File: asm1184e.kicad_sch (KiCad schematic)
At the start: 96 parts, among them J1 Bus_PCI_Express_x16, J2 Bus_PCI_Express_x16, J3 Bus_PCI_Express_x16, J4 Bus_PCI_Express_x16, J5 Bus_PCI_Express_x1, U12 ASM1184

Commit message: Add files via upload
version 1 done. hardware test and verification up next.
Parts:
- C10, C16: value 100n -> 12p
- R38: value 0 -> NC
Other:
- title: (none) -> asm1184e
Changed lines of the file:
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@@
 	(generator_version "9.0")
 	(paper "A3")
+	(title_block
+		(title "asm1184e")
+		(date "2025-04-09")
+		(rev "1")
+	)
 	(text "IS:\n0.1  -> 1A\n0.05 -> 2.5A\nFB:\n1.25V\n(1+R1/R2)*1.25=Vout"
 		(exclude_from_sim no)
@@
 			)
 		)
-		(property "Value" "100n"
+		(property "Value" "12p"
 			(at 69.342 224.79 90)
 			(effects
@@
 			)
 		)
-		(property "Value" "100n"
+		(property "Value" "12p"
 			(at 69.342 198.12 90)
 			(effects
@@
 		(dnp no)
 		(property "Reference" "R38"
-			(at 100.584 212.344 90)
+			(at 99.7575 212.34 90)
 			(effects
 				(font
@@
 			)
 		)
-		(property "Value" "0"
-			(at 99.822 214.63 90)
+		(property "Value" "NC"
+			(at 103.124 212.344 90)
 			(effects
 				(font
@@
 		(dnp no)
 		(property "Reference" "C15"
-			(at 60.452 215.9 90)
+			(at 61.0247 216.0039 90)
 			(effects
 				(font
@@
 		(dnp no)
 		(property "Reference" "C14"
-			(at 31.75 217.932 90)
+			(at 31.7992 218.8462 90)
 			(effects
 				(font
@@
 		(dnp no)
 		(property "Reference" "C18"
-			(at 96.901 217.8628 0)
+			(at 97.028 219.964 0)
 			(effects
 				(font
@@
 		)
 		(property "Value" "22u"
-			(at 96.901 220.2871 0)
+			(at 97.028 222.3883 0)
 			(effects
 				(font

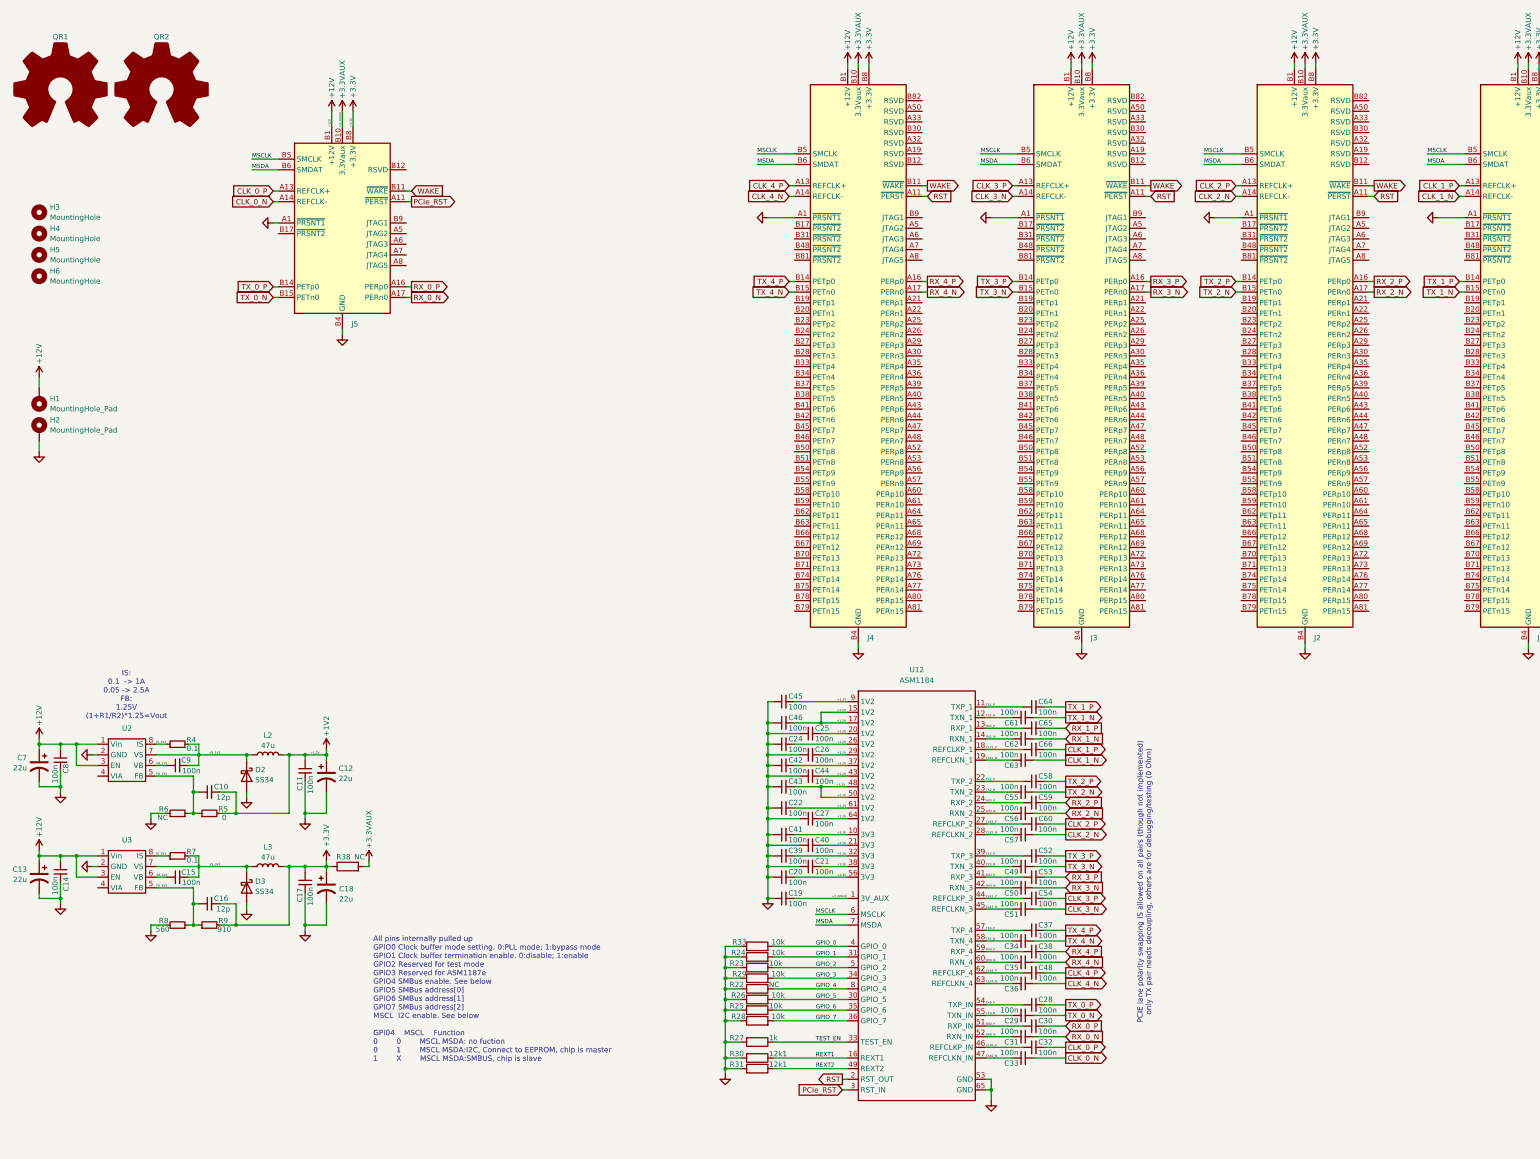
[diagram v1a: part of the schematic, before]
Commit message: added extra NC capacitors because why not.
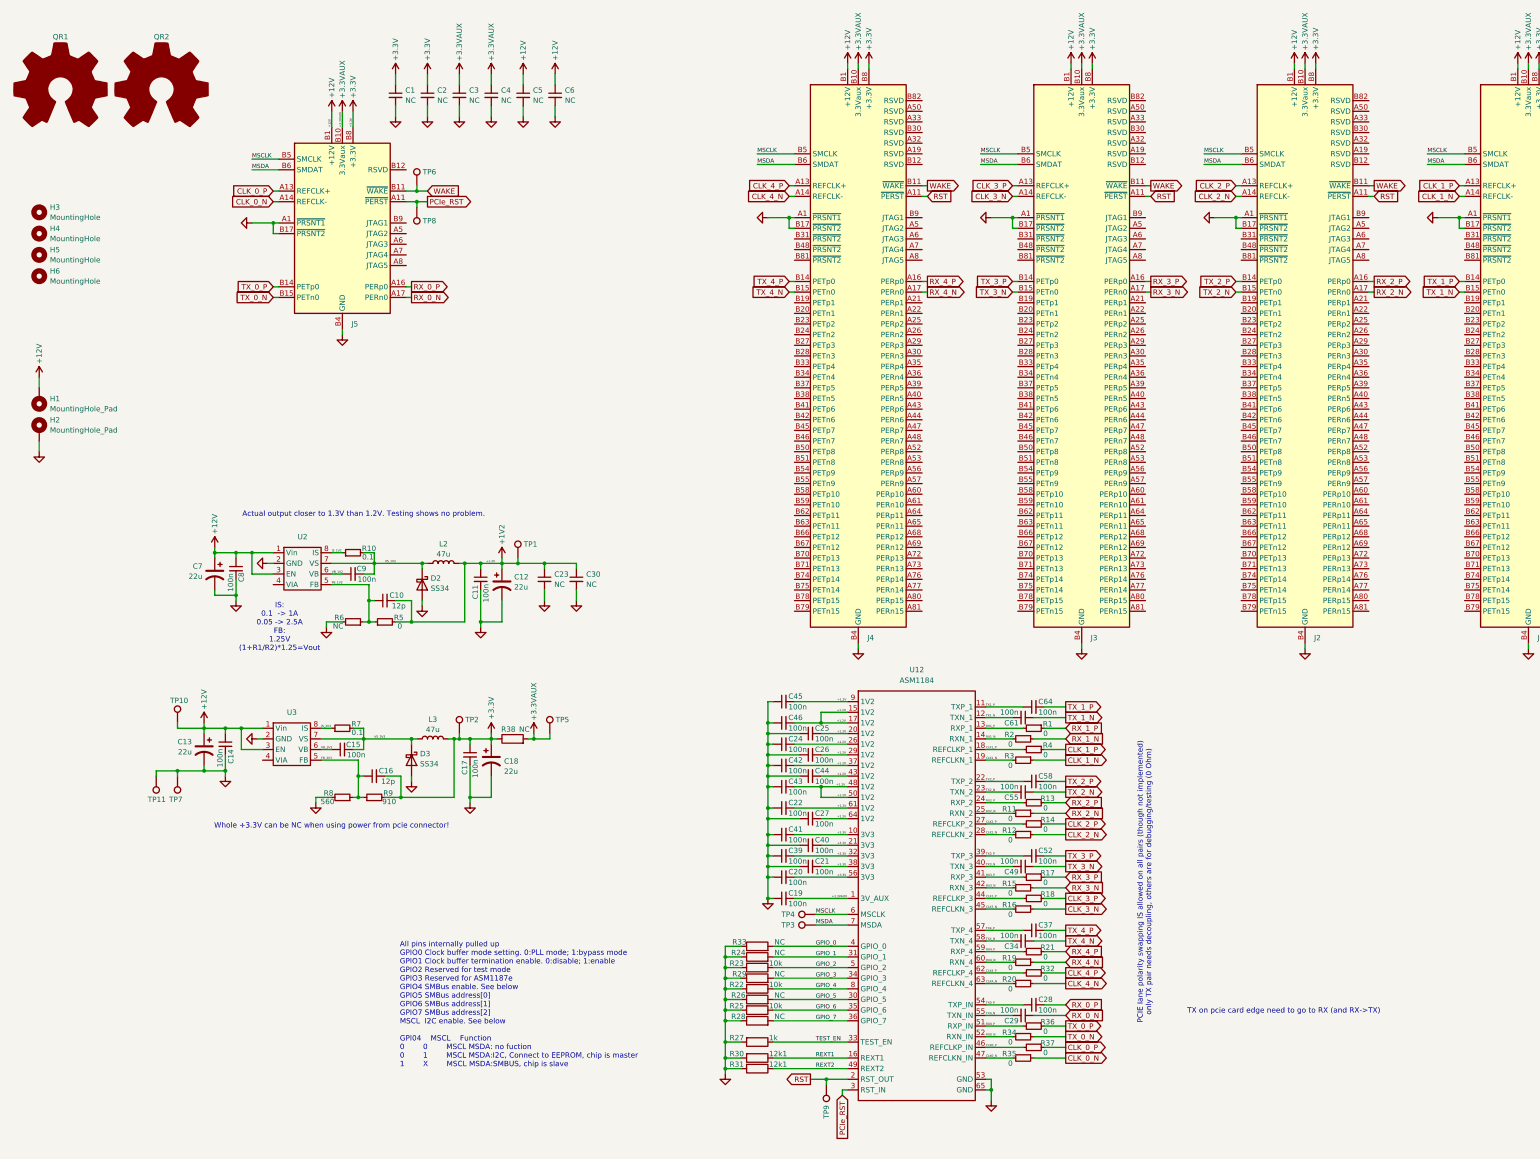
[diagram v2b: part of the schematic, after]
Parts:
- removed C31, C32, C33, C35, C36, C38, C48, C50, C51, C53, C54, C56, C57, C59, C60, C62, C63, C65, C66: 100n, Capacitor_SMD:C_0402_1005Metric, symbol Device:C_Small
- added C1, C2, C23, C3, C4, C5, C6: NC, Capacitor_SMD:C_0805_2012Metric, symbol Device:C_Small
- added R1, R11, R12, R13, R14, R15, R16, R17, R18, R19, R2, R20, R21, R3, R32, R34, R35, R36, R37, R4: 0, Resistor_SMD:R_0402_1005Metric, symbol Device:R_Small
- added TP1, TP10, TP11, TP2, TP3, TP4, TP5, TP6, TP7, TP8, TP9: TestPoint, TestPoint:TestPoint_Pad_D1.0mm, symbol Connector:TestPoint
- C30: value 100n -> NC; footprint Capacitor_SMD:C_0402_1005Metric -> Capacitor_SMD:C_0805_2012Metric
- R22: value NC -> 10k
- R24, R26, R28, R29, R33: value 10k -> NC
- renumbered R4 to R10
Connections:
- net +12V: now also C5.1, C6.1, TP10.1
- net +1V2: now also C30.1, C23.1, TP1.1
- net +3.3V: now also C1.1, C2.1, TP2.1
- net +3.3VAUX: now also C3.1, C4.1, TP5.1
- net CLK0_N: now also R35.2
- net CLK0_P: now also R37.2
- net CLK1_N: now also R3.2
- net CLK1_P: now also R4.2
- net CLK2_N: now also R12.2
- net CLK2_P: now also R14.2
- net CLK3_N: now also R16.2
- net CLK3_P: now also R18.2
- net CLK4_N: now also R20.2
- net CLK4_P: now also R32.2
- net CLK_0_N: now also R35.1
- net CLK_0_P: now also R37.1
- net CLK_1_N: now also R3.1
- net CLK_1_P: now also R4.1
- net CLK_2_N: now also R12.1
- net CLK_2_P: now also R14.1
- net CLK_3_N: now also R16.1
- net CLK_3_P: now also R18.1
- net CLK_4_N: now also R20.1
- net CLK_4_P: now also R32.1
- net GND: now also C30.2, J1.B17 (~{PRSNT2}), J2.B17 (~{PRSNT2}), J3.B17 (~{PRSNT2}), J4.B17 (~{PRSNT2}), J5.B17 (~{PRSNT2}), C1.2, C2.2, C23.2, C3.2, C4.2, C5.2, C6.2, TP11.1, TP7.1
- net MSCLK: now also TP4.1
- net MSDA: now also TP3.1
- net PCIe_RST: now also TP8.1
- net RST: now also TP9.1
- net RX0_N: now also R34.2
- net RX0_P: now also R36.2; no longer C30.1
- net RX1_N: now also R2.2
- net RX1_P: now also R1.2
- net RX2_N: now also R11.2
- net RX2_P: now also R13.2
- net RX3_N: now also R15.2
- net RX3_P: now also R17.2
- net RX4_N: now also R19.2
- net RX4_P: now also R21.2
- net RX_0_N: now also C29.1
- net RX_0_P: now also C28.2; no longer C30.2
- net RX_1_N: now also R2.1
- net RX_1_P: now also R1.1
- net RX_2_N: now also R11.1
- net RX_2_P: now also R13.1
- net RX_3_N: now also R15.1
- net RX_3_P: now also R17.1
- net RX_4_N: now also R19.1
- net RX_4_P: now also R21.1
- net TX_0_N: now also R34.1; no longer C29.1
- net TX_0_P: now also R36.1; no longer C28.2
- net WAKE: now also TP6.1
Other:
- note added: "Actual output closer to 1.3V than 1.2V. Testing shows no problem."
- note added: "TX on pcie card edge need to go to RX (and RX->TX)"
- note added: "Whole +3.3V can be NC when using power from pcie connector!"
- moved on the sheet: C10, C11, C12, C13, C14, C15, C16, C17, C18, C7, C8, C9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
